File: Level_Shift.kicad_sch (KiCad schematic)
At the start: 22 parts, among them U23 74AVC4T245, U25 74AVC4T245, U26 74LVC8T245, U27 74LVC8T245

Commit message: Routed LVDS lines
- Routed LVDS lines
- Swapped some digital output pairs
- Properly connected the output enable signal for digital outputs in the schematic
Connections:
- net OE_Digital_Outputs: now reaches U26.10 (A8)
- net OE_Digital_Outputs: now also U26.9 (A7)
- net OE_Digital_Outputs_B: now reaches U26.14 (B8)
- net OE_Digital_Outputs_A: now reaches U26.15 (B7)
- no-connect marks 12 -> 8
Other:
- note added: "TO DO: Likely want to GND unused gates"
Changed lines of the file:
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@@
 		)
 	)
+	(text "TO DO: Likely want to GND unused gates"
+		(exclude_from_sim no)
+		(at 293.878 195.834 0)
+		(effects
+			(font
+				(size 1.27 1.27)
+			)
+		)
+	)
 	(text "+2.5V"
 		(exclude_from_sim no)
@@
 	)
 	(junction
+		(at 146.05 171.45)
+		(diameter 0)
+		(color 0 0 0 0)
+	)
+	(junction
 		(at 355.6 38.1)
 		(diameter 0)
@@
 	)
 	(no_connect
-		(at 115.57 168.91)
-	)
-	(no_connect
-		(at 115.57 173.99)
-	)
-	(no_connect
-		(at 280.67 172.72)
-	)
-	(no_connect
-		(at 140.97 173.99)
-	)
-	(no_connect
-		(at 140.97 168.91)
-	)
-	(no_connect
 		(at 306.07 172.72)
 	)
 	(no_connect
-		(at 115.57 153.67)
+		(at 306.07 167.64)
 	)
 	(no_connect
-		(at 280.67 167.64)
+		(at 115.57 153.67)
 	)
 	(no_connect
@@
 	)
 	(no_connect
-		(at 306.07 167.64)
+		(at 280.67 172.72)
 	)
 	(no_connect
@@
 		(at 280.67 152.4)
 	)
+	(no_connect
+		(at 280.67 167.64)
+	)
 	(bus_entry
 		(at 53.34 95.25)
@@
 		)
 	)
+	(wire
+		(pts
+			(xy 146.05 168.91) (xy 140.97 168.91)
+		)
+		(stroke
+			(width 0)
+			(type default)
+		)
+	)
 	(bus
 		(pts
@@
 	(wire
 		(pts
+			(xy 106.68 168.91) (xy 115.57 168.91)
+		)
+		(stroke
+			(width 0)
+			(type default)
+		)
+	)
+	(wire
+		(pts
 			(xy 292.1 38.1) (xy 292.1 53.34)
 		)
@@
 	(wire
 		(pts
+			(xy 106.68 173.99) (xy 115.57 173.99)
+		)
+		(stroke
+			(width 0)
+			(type default)
+		)
+	)
+	(wire
+		(pts
 			(xy 288.29 110.49) (xy 293.37 110.49)
 		)
@@
 	(wire
 		(pts
+			(xy 146.05 173.99) (xy 146.05 171.45)
+		)
+		(stroke
+			(width 0)
+			(type default)
+		)
+	)
+	(wire
+		(pts
 			(xy 342.9 129.54) (xy 342.9 157.48)
 		)
@@
 		)
 	)
+	(wire
+		(pts
+			(xy 146.05 168.91) (xy 146.05 171.45)
+		)
+		(stroke
+			(width 0)
+			(type default)
+		)
+	)
 	(bus
 		(pts
@@
 	(wire
 		(pts
+			(xy 152.4 171.45) (xy 146.05 171.45)
+		)
+		(stroke
+			(width 0)
+			(type default)
+		)
+	)
+	(wire
+		(pts
 			(xy 190.5 60.96) (xy 190.5 63.5)
 		)
@@
 	(wire
 		(pts
+			(xy 140.97 173.99) (xy 146.05 173.99)
+		)
+		(stroke
+			(width 0)
+			(type default)
+		)
+	)
+	(wire
+		(pts
 			(xy 132.08 100.33) (xy 132.08 102.87)
 		)
@@
 		)
 	)
-	(label "OE_Faults"
+	(label "OE_Faults_1"
 		(at 344.17 62.23 0)
 		(effects
@@
 		)
 	)
+	(hierarchical_label "OE_Digital_Outputs"
+		(shape input)
+		(at 152.4 171.45 0)
+		(effects
+			(font
+				(size 1.27 1.27)
+			)
+			(justify left)
+		)
+	)
 	(hierarchical_label "OE_Faults_1"
 		(shape input)
@@
 		)
 	)
+	(hierarchical_label "OE_Digital_Outputs_A"
+		(shape output)
+		(at 106.68 168.91 180)
+		(effects
+			(font
+				(size 1.27 1.27)
+			)
+			(justify right)
+		)
+	)
+	(hierarchical_label "OE_Digital_Outputs_B"
+		(shape output)
+		(at 106.68 173.99 180)
+		(effects
+			(font
+				(size 1.27 1.27)
+			)
+			(justify right)
+		)
+	)

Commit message: Schematic and Layout Tweaks
- Updated all vias to 0.6/0.3mm
- New mechanical universal Marble holes for H2
- widen the power traces to Test points
- Add pin 4 of U20/U24 to GND net
- add a GND pour around U44 for heat
- Widen GND traces on LDOs (U24/U20)
- Grounding of unused gates of level shifters
-Small updates footprints for U18,U19,U23,U25
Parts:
- U23, U25: footprint Package_SO:TSSOP-16_4.4x5mm_P0.65mm -> rf-input-fmc:TSSOP-16_4.4x5mm_P0.65mm
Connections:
- net GND: now also U26.6 (A4), U27.10 (A8), U27.6 (A4), U27.9 (A7)
- no-connect marks 8 -> 4

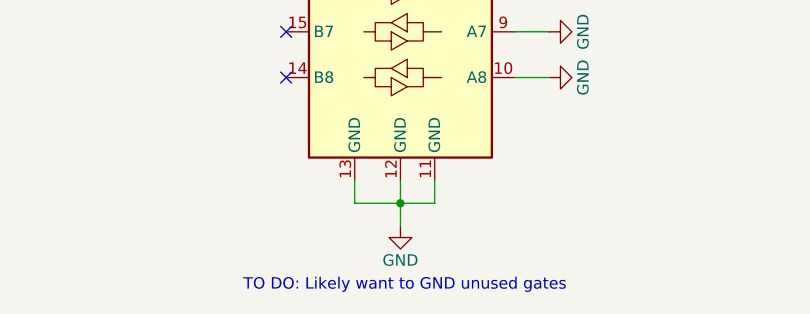
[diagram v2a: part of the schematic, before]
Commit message: Updated Layout of XOs and Digital Output Sections
- Added some additional comments to schematics (Y1&Y2)
- Added additional ground vias around U44
- Add GND planes around 1.8V LDOs (U21&U28)
- Straightened out some power routing tracks with 90deg bends
- Revised routing of Y1&Y2
- Revised routing of each digital output section
- All DCR/ERC errors resolved.
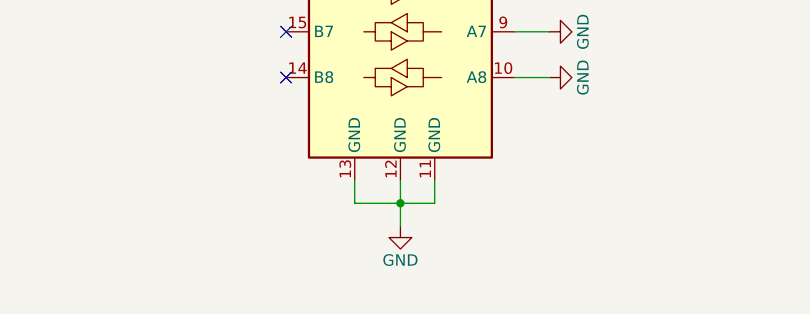
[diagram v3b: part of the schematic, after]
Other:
- note removed: "TO DO: Likely want to GND unused gates"
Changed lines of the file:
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@@
-		)
-	)
-	(text "TO DO: Likely want to GND unused gates"
-		(exclude_from_sim no)
-		(at 293.878 195.834 0)
-		(effects
-			(font
-				(size 1.27 1.27)
-			)
 		)
 	)

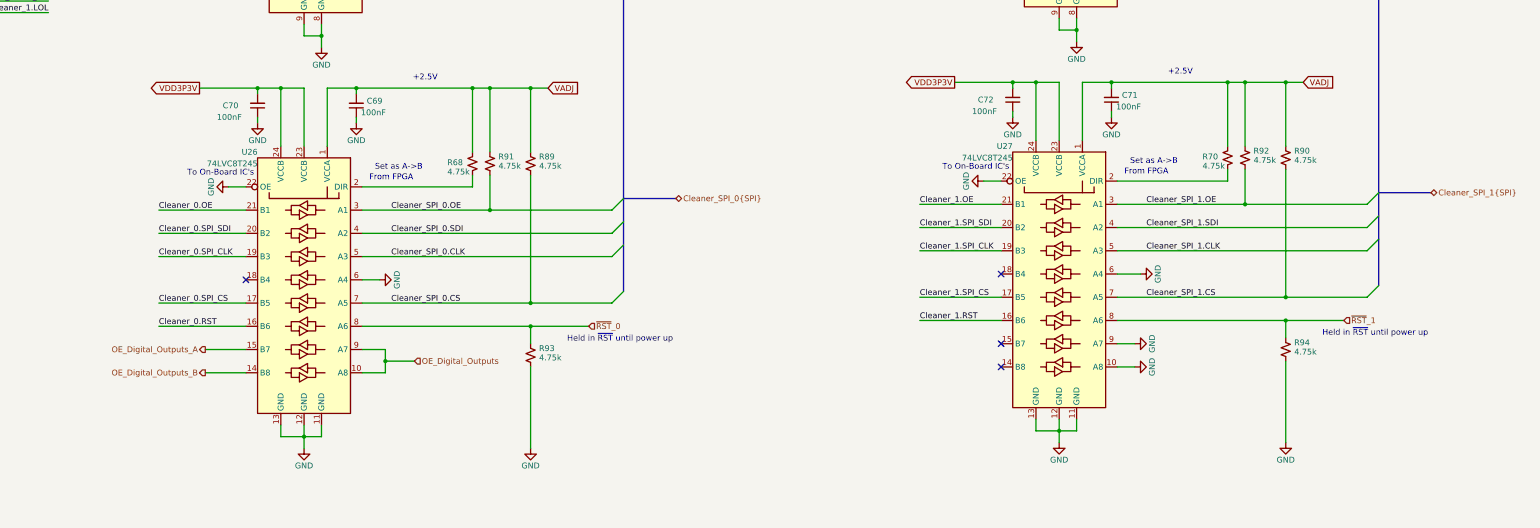
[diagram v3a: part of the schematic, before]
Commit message: Updates after external review
- Removed various construction lines on comments layer
- Corrected various 50ohm SE traces on external layers to 0.26mm width
- Shortened up longer traces where possible on external layers and LVDS (in5)
- Made routing of CLK signals to MMCX test ports consistant

- MAJOR UPDATE to XTAL (Y1&Y2)
This now follows the family reference manual to properly isolate the XTAL
This then required the following changes:
- Swapped layer In2 with In5 (to keep LVDS between GND layers)
- Swapped layer In3 with In4 (to keep LVDS between GND layers)
- Revised gate mapping of level shifted signals on the IC (no FMC pinout change)
- Significant revision to  routing around these area
- Rounded XTAL pads
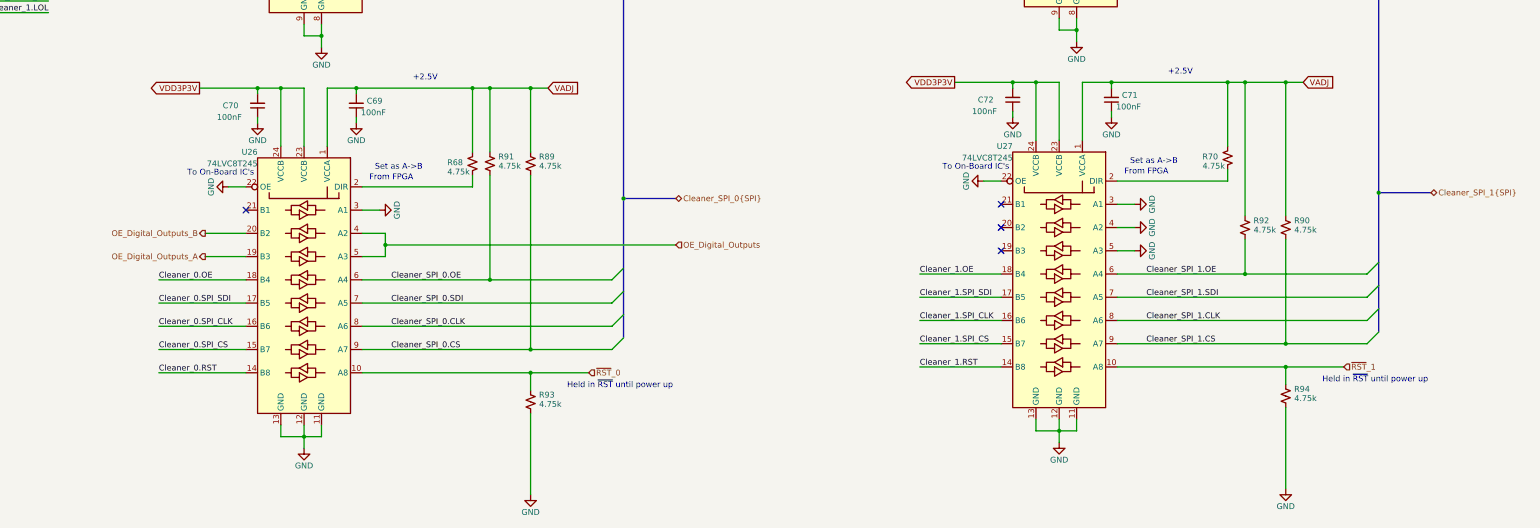
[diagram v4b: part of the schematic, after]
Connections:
- net Cleaner_0.OE: now also U26.18 (B4); no longer U26.21 (B1)
- net Cleaner_0.RST: now also U26.14 (B8); no longer U26.16 (B6)
- net Cleaner_0.SPI_CLK: now also U26.16 (B6); no longer U26.19 (B3)
- net Cleaner_0.SPI_CS: now also U26.15 (B7); no longer U26.17 (B5)
- net Cleaner_0.SPI_SDI: now also U26.17 (B5); no longer U26.20 (B2)
- net Cleaner_1.OE: now also U27.18 (B4); no longer U27.21 (B1)
- net Cleaner_1.RST: now also U27.14 (B8); no longer U27.16 (B6)
- net Cleaner_1.SPI_CLK: now also U27.16 (B6); no longer U27.19 (B3)
- net Cleaner_1.SPI_CS: now also U27.15 (B7); no longer U27.17 (B5)
- net Cleaner_1.SPI_SDI: now also U27.17 (B5); no longer U27.20 (B2)
- net Cleaner_SPI_0.CLK: now also U26.8 (A6); no longer U26.5 (A3)
- net Cleaner_SPI_0.CS: now also U26.9 (A7); no longer U26.7 (A5)
- net Cleaner_SPI_0.OE: now also U26.6 (A4); no longer U26.3 (A1)
- net Cleaner_SPI_0.SDI: now also U26.7 (A5); no longer U26.4 (A2)
- net Cleaner_SPI_1.CLK: now also U27.8 (A6); no longer U27.5 (A3)
- net Cleaner_SPI_1.CS: now also U27.9 (A7); no longer U27.7 (A5)
- net Cleaner_SPI_1.OE: now also U27.6 (A4); no longer U27.3 (A1)
- net Cleaner_SPI_1.SDI: now also U27.7 (A5); no longer U27.4 (A2)
- net GND: now also U26.3 (A1), U27.3 (A1), U27.4 (A2), U27.5 (A3); no longer U26.6 (A4), U27.10 (A8), U27.6 (A4), U27.9 (A7)
- net OE_Digital_Outputs: now also U26.4 (A2), U26.5 (A3); no longer U26.10 (A8), U26.9 (A7)
- net OE_Digital_Outputs_A: now also U26.19 (B3); no longer U26.15 (B7)
- net OE_Digital_Outputs_B: now also U26.20 (B2); no longer U26.14 (B8)
- net ~{RST}_0: now also U26.10 (A8); no longer U26.8 (A6)
- net ~{RST}_1: now also U27.10 (A8); no longer U27.8 (A6)
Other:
- moved on the sheet: R90, R92, R93, R94
